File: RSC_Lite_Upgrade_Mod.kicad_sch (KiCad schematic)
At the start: 3 parts, among them J1 USB_B_Micro, U1 STM32F103C8Tx

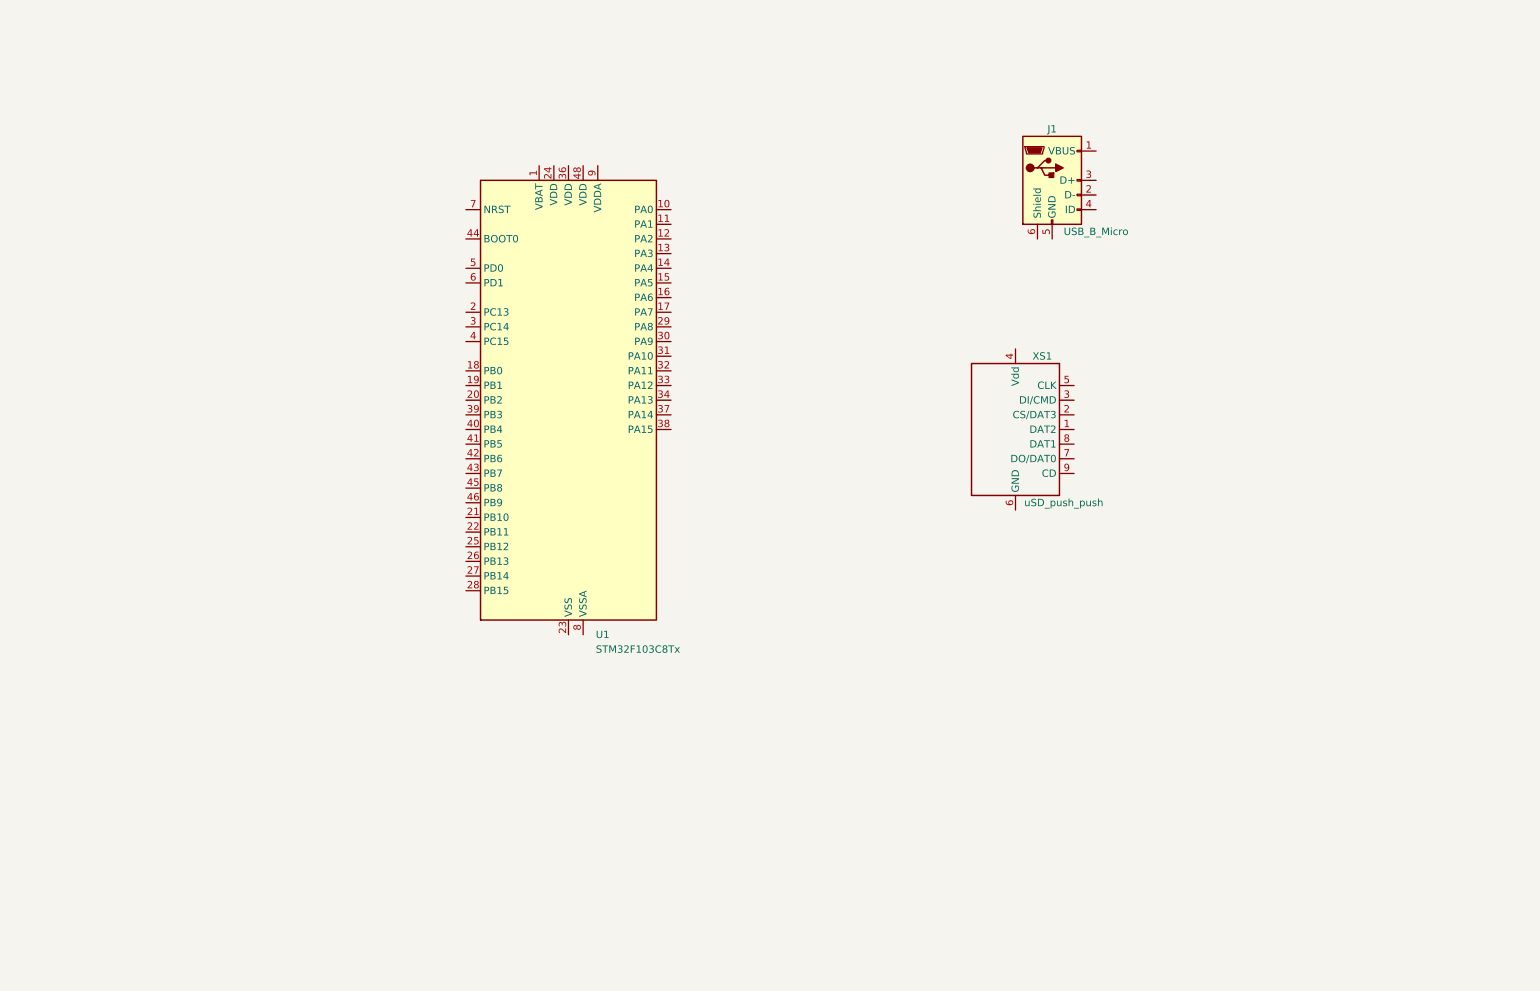
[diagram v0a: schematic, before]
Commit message: Begin drawing the RSC Lite upgrade mod circuit
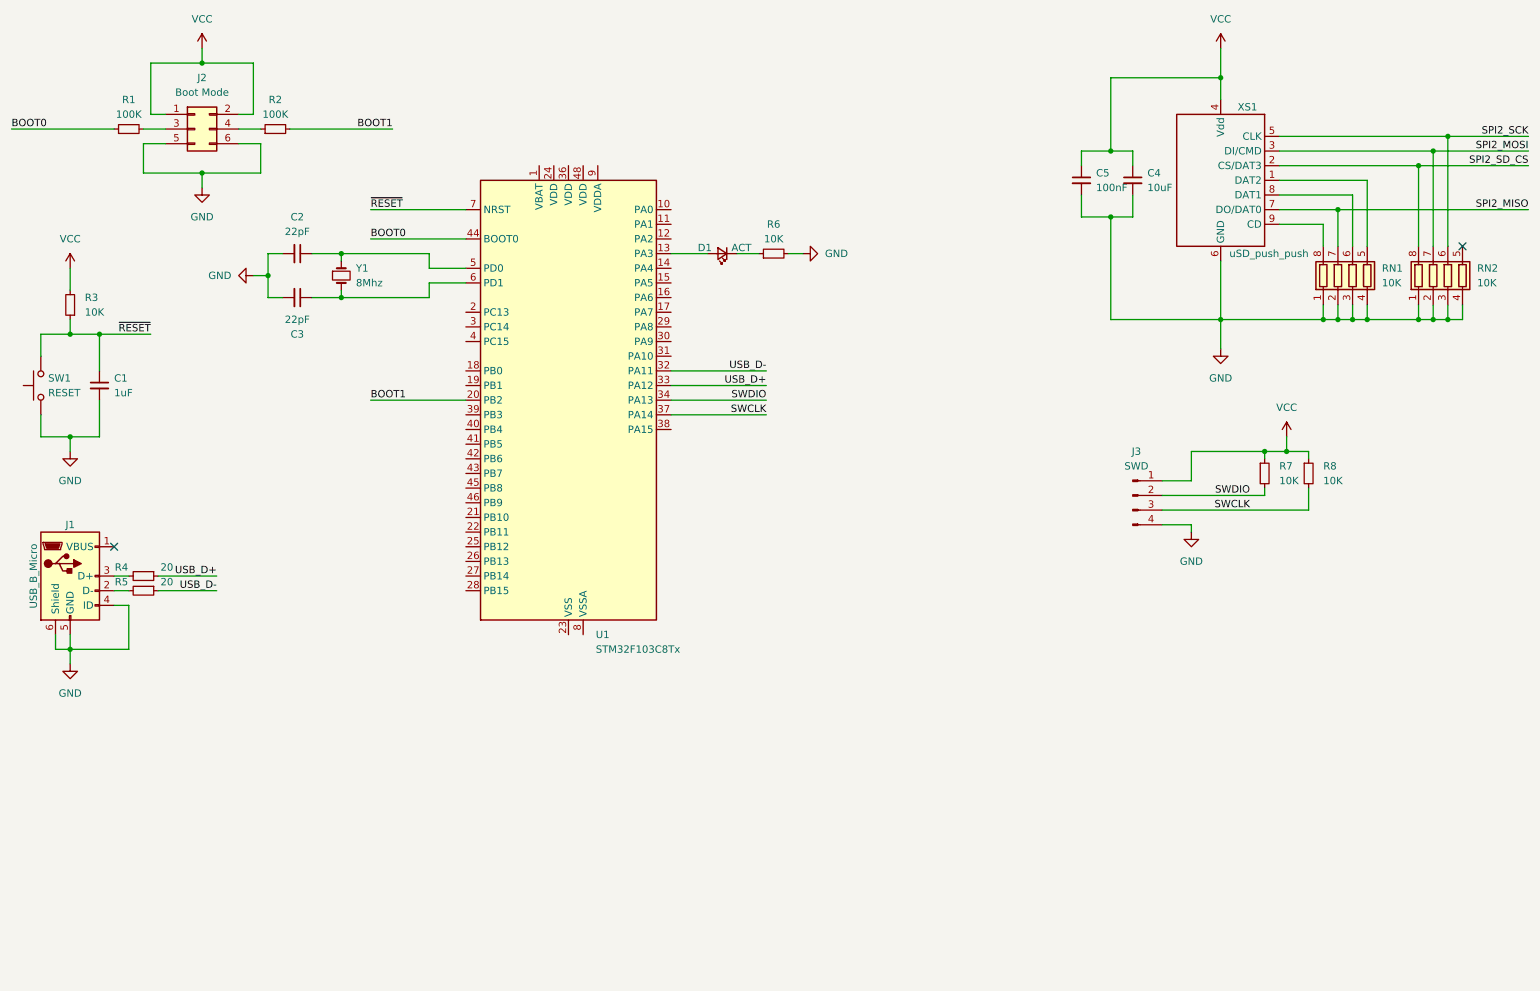
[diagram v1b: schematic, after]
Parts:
- added C1: 1uF, symbol Device:C_Small
- added C2, C3: 22pF, symbol Device:C_Small
- added C4: 10uF, symbol Device:C_Small
- added C5: 100nF, symbol Device:C_Small
- added D1: ACT, symbol Device:LED_Small
- added J2: Boot Mode, symbol Connector_Generic:Conn_02x03_Odd_Even
- added J3: SWD, symbol Connector:Conn_01x04_Pin
- added R1, R2: 100K, symbol Device:R_Small
- added R3, R6, R7, R8: 10K, symbol Device:R_Small
- added R4, R5: 20, symbol Device:R_Small
- added RN1, RN2: 10K, symbol Device:R_Pack04
- added SW1: RESET, symbol Switch:SW_Push
- added Y1: 8Mhz, symbol Device:Crystal_Small
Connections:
- net at J1.2 (D-): now also R5.2
- net at J1.3 (D+): now also R4.2
- net GND: now reaches J1.4 (ID)
- net GND: now also J1.5 (GND), J1.6 (Shield), XS1.6 (GND), C1.2, C2.2, C3.2, C4.2, C5.2, J2.5 (Pin_5), J2.6 (Pin_6), J3.4 (Pin_4), R6.2, RN1.1 (R1.1), RN1.2 (R2.1), RN1.3 (R3.1), RN1.4 (R4.1), RN2.1 (R1.1), RN2.2 (R2.1), RN2.3 (R3.1), RN2.4 (R4.1), SW1.1
- net at XS1.1 (DAT2): now also RN1.5 (R4.2)
- net SPI2_SD_CS: now reaches XS1.2 (CS/DAT3)
- net SPI2_SD_CS: now also RN2.8 (R1.2)
- net SPI2_MOSI: now reaches XS1.3 (DI/CMD)
- net SPI2_MOSI: now also RN2.7 (R2.2)
- net VCC: now reaches XS1.4 (Vdd)
- net VCC: now also C4.1, C5.1, J2.1 (Pin_1), J2.2 (Pin_2), J3.1 (Pin_1), R3.2, R7.1, R8.1
- net SPI2_SCK: now reaches XS1.5 (CLK)
- net SPI2_SCK: now also RN2.6 (R3.2)
- net SPI2_MISO: now reaches XS1.7 (DO/DAT0)
- net SPI2_MISO: now also RN1.7 (R2.2)
- net at XS1.8 (DAT1): now also RN1.6 (R3.2)
- net at XS1.9 (CD): now also RN1.8 (R1.2)
- net at U1.13 (PA3): now also D1.2 (A)
- net BOOT1: now reaches U1.20 (PB2)
- net BOOT1: now also R2.2
- net USB_D-: now reaches U1.32 (PA11)
- net USB_D-: now also R5.1
- net USB_D+: now reaches U1.33 (PA12)
- net USB_D+: now also R4.1
- net SWDIO: now reaches U1.34 (PA13)
- net SWDIO: now also J3.2 (Pin_2), R7.2
- net SWCLK: now reaches U1.37 (PA14)
- net SWCLK: now also J3.3 (Pin_3), R8.2
- net BOOT0: now reaches U1.44 (BOOT0)
- net BOOT0: now also R1.1
- net at U1.5 (PD0): now also C2.1, Y1.1
- net at U1.6 (PD1): now also C3.1, Y1.2
- net ~{RESET}: now reaches U1.7 (NRST)
- net ~{RESET}: now also C1.1, R3.1, SW1.2
- new net: J2.4 (Pin_4), R2.1
- new net: J2.3 (Pin_3), R1.2
- new net: D1.1 (K), R6.1
- no-connect marks 0 -> 2
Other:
- moved on the sheet: J1, XS1

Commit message: Update schematics
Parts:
- added C10, C6, C7, C8, C9: 100nF, symbol Device:C_Small
- added C11: 10uF, symbol Device:C_Small
- added J4: JTAG, symbol Connector:Conn_01x06_Pin
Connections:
- net GND: now also U1.23 (VSS), U1.35 (VSS), U1.47 (VSS), U1.8 (VSSA), C10.2, C11.2, C6.2, C7.2, C8.2, C9.2, J4.2 (Pin_2)
- net SPI2_MISO: now also U1.27 (PB14)
- net SPI2_MOSI: now also U1.28 (PB15)
- net SPI2_SCK: now also U1.26 (PB13)
- net SPI2_SD_CS: now also U1.25 (PB12)
- net VCC: now also U1.1 (VBAT), U1.24 (VDD), U1.36 (VDD), U1.48 (VDD), U1.9 (VDDA), C10.1, C11.1, C6.1, C7.1, C8.1, C9.1, J4.1 (Pin_1)
- net JTAG_TDO: now reaches U1.41 (PB5)
- net JTAG_TDO: now also J4.3 (Pin_3)
- net JTAG_TDI: now reaches U1.42 (PB6)
- net JTAG_TDI: now also J4.5 (Pin_5)
- net JTAG_TCK: now reaches U1.43 (PB7)
- net JTAG_TCK: now also J4.4 (Pin_4)
- net JTAG_TMS: now reaches U1.45 (PB8)
- net JTAG_TMS: now also J4.6 (Pin_6)
- no-connect marks 2 -> 23
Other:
- moved on the sheet: C2, C3, D1, J2, J3, R1, R2, R6, R7, R8, U1, Y1

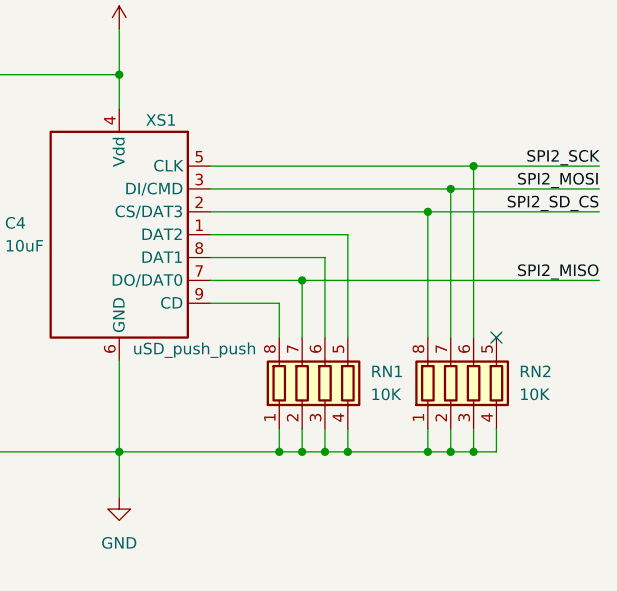
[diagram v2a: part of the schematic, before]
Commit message: Basic routing for the board
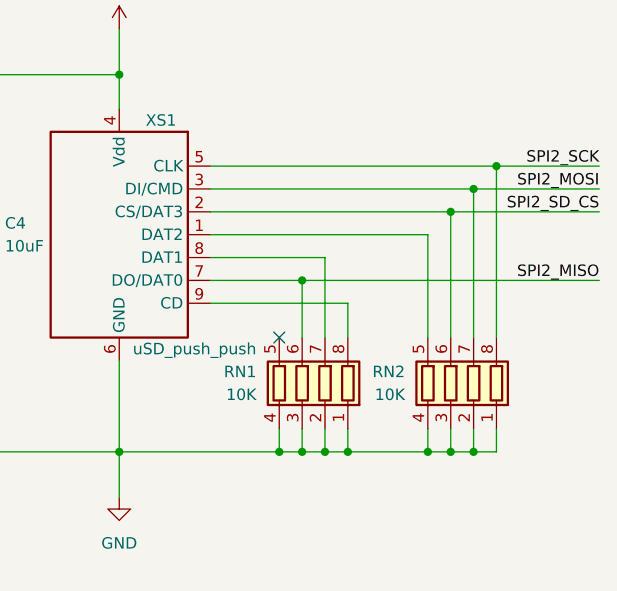
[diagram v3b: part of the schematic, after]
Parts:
- C1, C10, C11, C2, C3, C4, C5, C6, C7, C8, C9: footprint (none) -> Capacitor_SMD:C_1206_3216Metric_Pad1.33x1.80mm_HandSolder
- D1: footprint (none) -> LED_SMD:LED_1206_3216Metric
- J2: footprint (none) -> Connector_PinHeader_2.54mm:PinHeader_2x03_P2.54mm_Vertical
- J3: footprint (none) -> Connector_PinHeader_2.54mm:PinHeader_1x04_P2.54mm_Vertical
- J4: footprint (none) -> Connector_PinHeader_2.54mm:PinHeader_1x06_P2.54mm_Horizontal
- R1, R2, R3, R4, R5, R6, R7, R8: footprint (none) -> Resistor_SMD:R_1206_3216Metric_Pad1.30x1.75mm_HandSolder
- RN1, RN2: footprint (none) -> Resistor_SMD:R_Array_Convex_4x0612
- SW1: footprint (none) -> Button_Switch_THT:SW_PUSH_6mm
- Y1: footprint (none) -> Crystal:Crystal_SMD_HC49-SD
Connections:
- net SPI2_MISO: now also RN1.6 (R3.2); no longer RN1.7 (R2.2)
- net SPI2_SCK: now also RN2.8 (R1.2); no longer RN2.6 (R3.2)
- net SPI2_SD_CS: now also RN2.6 (R3.2); no longer RN2.8 (R1.2)
- net at RN1.5 (R4.2): no longer XS1.1 (DAT2)
- net at XS1.8 (DAT1): now also RN1.7 (R2.2); no longer RN1.6 (R3.2)
- net at RN2.5 (R4.2): now also XS1.1 (DAT2)

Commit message: Add gerbers and firmware for revision 1
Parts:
- added R9: 1.5K, Resistor_SMD:R_1206_3216Metric_Pad1.30x1.75mm_HandSolder, symbol Device:R_Small
- C1: value 1uF -> 100nF
- R6: value 10K -> 1K
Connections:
- net GND: no longer RN1.1 (R1.1), RN1.2 (R2.1), RN1.3 (R3.1), RN1.4 (R4.1), RN2.1 (R1.1), RN2.2 (R2.1), RN2.3 (R3.1), RN2.4 (R4.1)
- net USB_D+: now also R9.2
- net VCC: now also RN1.1 (R1.1), RN1.2 (R2.1), RN1.3 (R3.1), RN1.4 (R4.1), RN2.1 (R1.1), RN2.2 (R2.1), RN2.3 (R3.1), RN2.4 (R4.1)
- net USB_PULL: now reaches U1.29 (PA8)
- net USB_PULL: now also R9.1
- no-connect marks 23 -> 22

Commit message: Merge resized rev.2 board
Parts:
- removed C10: 100nF, Capacitor_SMD:C_1206_3216Metric_Pad1.33x1.80mm_HandSolder, symbol Device:C_Small
- removed J1: USB_B_Micro, mod:Conn_USBmicro-B_ebay-side_TH, symbol KungFuFlash-rescue:USB_B_Micro-Connector
- removed J2: Boot Mode, Connector_PinHeader_2.54mm:PinHeader_2x03_P2.54mm_Vertical, symbol Connector_Generic:Conn_02x03_Odd_Even
- removed R1, R2: 100K, Resistor_SMD:R_1206_3216Metric_Pad1.30x1.75mm_HandSolder, symbol Device:R_Small
- removed R4, R5: 20, Resistor_SMD:R_1206_3216Metric_Pad1.30x1.75mm_HandSolder, symbol Device:R_Small
- removed R9: 1.5K, Resistor_SMD:R_1206_3216Metric_Pad1.30x1.75mm_HandSolder, symbol Device:R_Small
- removed SW1: RESET, Button_Switch_THT:SW_PUSH_6mm, symbol Switch:SW_Push
- C1, C2, C3, C4, C5, C6, C7, C8, C9: footprint Capacitor_SMD:C_1206_3216Metric_Pad1.33x1.80mm_HandSolder -> Capacitor_SMD:C_0805_2012Metric_Pad1.18x1.45mm_HandSolder
- C10: renamed from C11; footprint Capacitor_SMD:C_1206_3216Metric_Pad1.33x1.80mm_HandSolder -> Capacitor_SMD:C_0805_2012Metric_Pad1.18x1.45mm_HandSolder
- D1: footprint LED_SMD:LED_1206_3216Metric -> LED_SMD:LED_0805_2012Metric_Pad1.15x1.40mm_HandSolder
- R3, R6, R7, R8: footprint Resistor_SMD:R_1206_3216Metric_Pad1.30x1.75mm_HandSolder -> Resistor_SMD:R_0805_2012Metric_Pad1.20x1.40mm_HandSolder
- U1: value STM32F103C8Tx -> 32F103C8T6
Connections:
- net BOOT0 is gone; now on net GND: U1.44 (BOOT0)
- net GND: now also J4.5 (Pin_5); no longer J4.2 (Pin_2)
- net JTAG_TCK: now also J4.3 (Pin_3); no longer J4.4 (Pin_4)
- net JTAG_TDI: now also J4.2 (Pin_2); no longer J4.5 (Pin_5)
- net JTAG_TDO: now also J4.4 (Pin_4); no longer J4.3 (Pin_3)
- net JTAG_TMS: now also J4.1 (Pin_1); no longer J4.6 (Pin_6)
- net VCC: now also J4.6 (Pin_6); no longer J4.1 (Pin_1)
- net USB_PULL: no longer names the net of U1.29 (PA8)
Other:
- moved on the sheet: C1, C10, C2, C3, D1, R6, U1, Y1
